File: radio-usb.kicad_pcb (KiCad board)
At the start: 2 copper layers, 127 x 90 mm, 228 parts, among them J1 Barrel_Jack, J10 Conn_Coaxial, J11 ACJS-MHDRM, J12 ACJS-MHDRM, J2 miniUSB, J3 15EDGRC-3.5-03P-14, J4 DB9_Female, J5 EEP_EN, J6 Mini-DIN-6, J7 EDAC 690-008-221-904, J8 DB9_Male, J9 Conn_Coaxial, Q1 BC846C, Q2 BC846, Q3 BC846, Q4 BC846, Q5 BC856, SW1 SW_Push_DPDT, SW2 SW_SPDT, SW3 SW_SPDT, SW4 SW_DIP_x04, SW5 SW_DIP_x04, SW6 SW_DPDT_x2, SW7 SW_SPDT, U1 L7805, U10 AP2171W, U11 TLP2662, U12 TLP2662, U13 MAX3232, U14 93CxxC, U15 PCM2902, U17 FT2232HL, U18 PC817, U19 CRIYCHLEY9000, U2 24LC04, U20 PC817, U21 PC817, U22 CRIYCHLEY9000, U23 LMV321IDBVR, U3 APX809_810-xxSA, U4 AP22814AW5, U5 AP22814AW5, U6 USB2514B_Bi, U7 LM1117-3.3, U8 TBA 1-0511, U9 4069, X1 MAB5SH, Y1 24MHz, Y2 12MHz, Y3 12M

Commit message: almost everything routed
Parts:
- moved TP8 32.2 mm to (174.0, 74.5)
- moved R71 20.4 mm to (115.1, 49.1), turned to 180 degrees
- moved R45 1.86 mm to (108.5, 49.8)
- moved C37 1.85 mm to (114.8, 43.9)
- moved C48 1.22 mm to (109.1, 64.6)
- moved R68 0.66 mm to (111.3, 64.8)
- moved Q4 0.57 mm to (133.5, 69.5)
- moved R63 0.49 mm to (134.1, 73.5)
- moved C39 0.45 mm to (117.2, 44.9)
- moved R53 0.40 mm to (111.8, 43.4)
- moved R72 0.36 mm to (111.3, 48.8)
- moved R64 0.33 mm to (111.3, 46.8)
- moved C62 0.20 mm to (124.4, 72.7)
- moved R66 0.05 mm to (122.3, 77.2)
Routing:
- net GND: track 298.3 -> 574.2 mm, vias 75 -> 93
- net GNDREF: track 144.4 -> 226.2 mm, vias 7 -> 9
- net /PTT_ACTL: track 0.00 -> 76.4 mm, vias 0 -> 1
- net RX_ACTIVE: track 15.3 -> 77.8 mm, vias 1 -> 3
- net /PTT_ACTH: track 0.00 -> 57.3 mm, vias 0 -> 3
- net /AF_FRM_RADIO_PREINS: track 68.4 -> 125.3 mm, vias 1 -> 4
- net /AUD_IN_SUM: track 69.5 -> 119.8 mm, vias 1 -> 4
- net /AUD_VDDI: track 0.00 -> 40.2 mm, vias 0 -> 2
- net /RX_ACT_SEP: track 27.4 -> 65.9 mm, vias 1 -> 4
- net /RCA_LEFT: track 50.5 -> 87.4 mm, vias 0 -> 3
- net /AUD_VBUS: track 8.70 -> 44.3 mm, vias 0 -> 2
- net /RCA_RIGHT: track 43.2 -> 78.8 mm, vias 0 -> 1
- net Net-(Q4-Pad3): track 9.07 -> 42.9 mm, vias 1 -> 5
- net VD: track 126.6 -> 155.6 mm, vias 4 -> 7
- net Net-(C63-Pad1): track 64.6 -> 90.0 mm, vias 0 -> 1
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
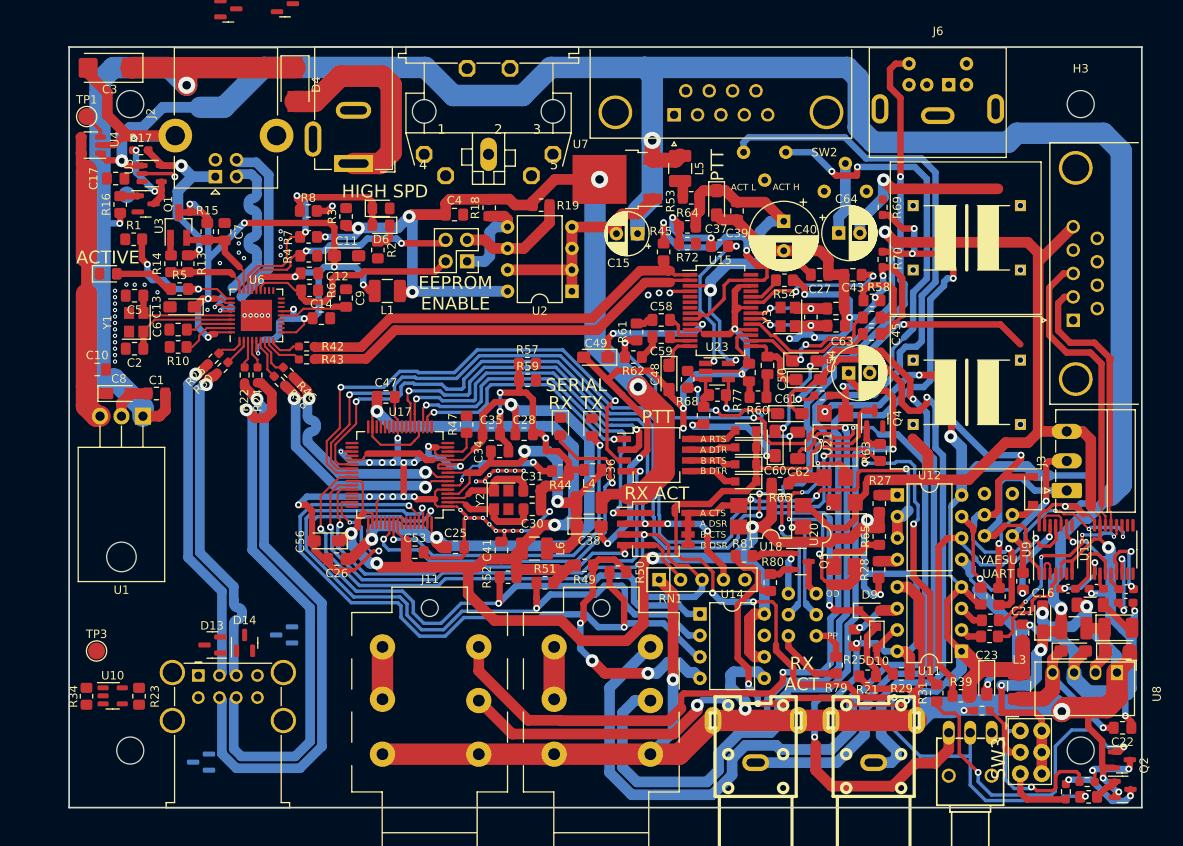
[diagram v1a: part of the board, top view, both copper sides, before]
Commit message: everything but ground poluygon and fixed bourns trafo pinout
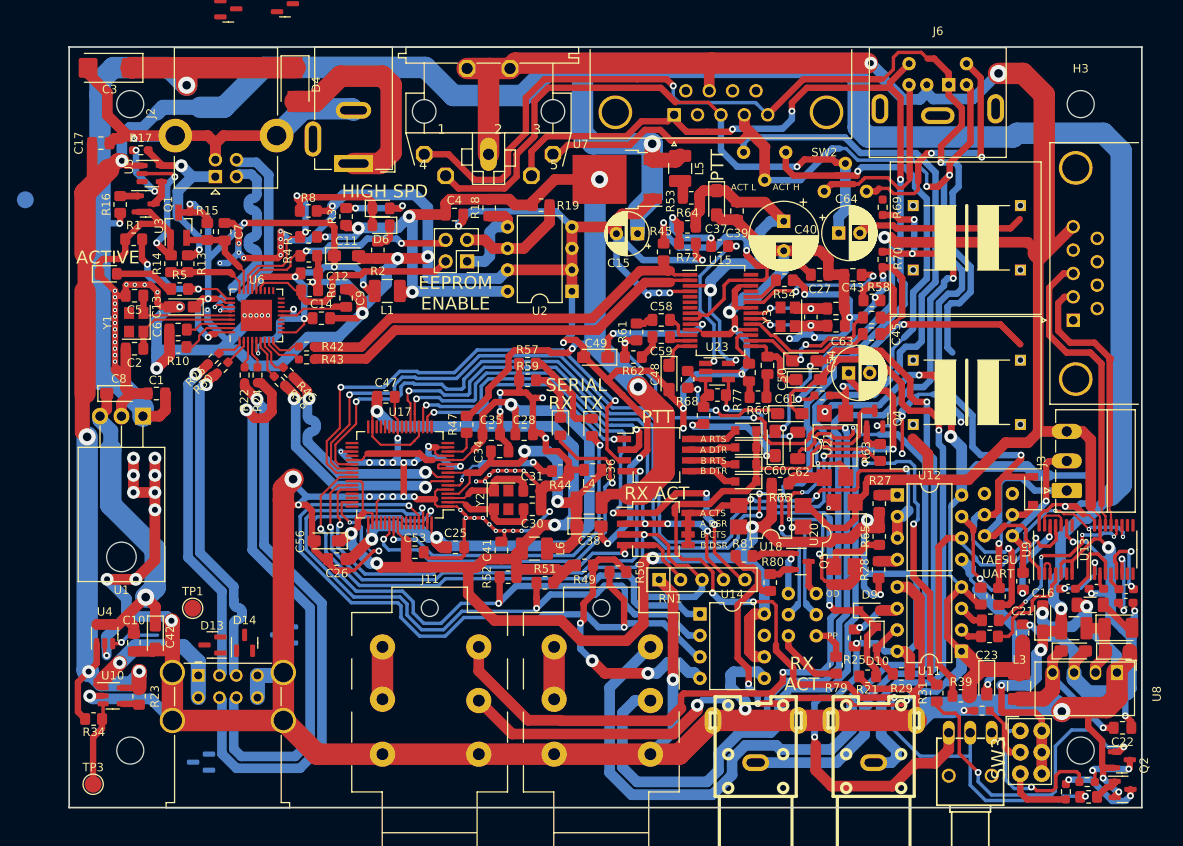
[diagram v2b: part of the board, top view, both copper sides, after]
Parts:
- added C42: 22u, Capacitor_Tantalum_SMD:CP_EIA-3216-18_Kemet-A_Pad1.58x1.35mm_HandSolder, F.Cu at (48.3, 95.4)
- moved TP1 59.6 mm to (52.7, 91.9)
- moved U4 57.9 mm to (42.3, 95.0), turned to 90 degrees
- moved C10 32.6 mm to (45.8, 96.0), turned to -90 degrees
- moved TP3 15.8 mm to (40.9, 112.8)
- moved TP2 12.0 mm to (32.9, 43.6)
- moved C17 4.54 mm to (41.9, 36.9)
- moved R34 2.82 mm to (41.0, 105.1), turned to 0 degrees
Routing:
- net GND: track 574.2 -> 1032.9 mm, vias 93 -> 122
- net AF_TO_RADIO: track 0.00 -> 119.4 mm, vias 0 -> 2
- net GNDREF: track 226.2 -> 332.4 mm, vias 9 -> 11
- net PTT: track 47.5 -> 146.4 mm, vias 2 -> 4
- net +5V: track 256.5 -> 351.4 mm, vias 5 -> 8
- net AF_FRM_RADIO: track 8.57 -> 72.3 mm, vias 0 -> 1
- net RX_ACTIVE: track 77.8 -> 128.4 mm, vias 3 -> 5
- net /YAESU_FILTERED_AUD: track 0.00 -> 30.4 mm, vias 0 -> 2
- net /YAESU_FLAT_AUD: track 0.00 -> 23.0 mm
- net +5VP: track 0.00 -> 22.4 mm, vias 0 -> 1
- net +3V3: track 109.0 -> 129.4 mm, vias 6 -> 7
- net /SER_A_CTS_IN: track 45.8 -> 65.9 mm, vias 2 -> 4
- net Net-(D15-Pad1): track 0.00 -> 10.8 mm
- net /+5VP_OK: track 0.00 -> 10.0 mm
- net Net-(D5-Pad2): track 0.00 -> 8.44 mm, vias 0 -> 2
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
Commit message: everything routed, bourns audio transformer footprint correcred, ground polygons
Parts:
- removed D11, D13, D14, D2, D3, D8: CM1213A-01SO, Package_TO_SOT_SMD:SOT-23
- added R56: 2k2, Resistor_SMD:R_0805_2012Metric_Pad1.20x1.40mm_HandSolder, B.Cu at (159.5, 72.7)
- TP1, TP6: footprint TestPoint:TestPoint_Pad_D2.0mm -> TestPoint:TestPoint_Pad_D1.0mm; moved to B.Cu
- TP2, TP4, TP5, TP9: footprint TestPoint:TestPoint_Pad_D2.0mm -> TestPoint:TestPoint_Pad_D1.0mm
- moved TP6 332.8 mm to (148.3, 88.6), turned to 180 degrees
- moved TP9 47.2 mm to (134.0, 94.5)
- moved TP8 40.5 mm to (133.6, 76.9)
- moved TP7 27.1 mm to (146.7, 95.5)
- moved TP5 23.9 mm to (151.0, 92.5)
- moved TP4 17.7 mm to (161.5, 81.2)
- moved TP2 11.6 mm to (44.5, 43.2)
- moved TP1 2.52 mm to (52.0, 94.4), turned to 180 degrees
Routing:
- net GND: track 1032.9 -> 1095.0 mm, vias 122 -> 123
- net /CAT_UART_RX: track 27.3 -> 43.9 mm, vias 0 -> 2
- net GNDREF: track 332.4 -> 341.3 mm
- net AF_TO_RADIO: track 119.4 -> 124.4 mm, vias 2 -> 3
- net Net-(TP2-Pad1): track 0.00 -> 4.69 mm, vias 0 -> 1
- net /SER_B_TXD_OUT: track 113.0 -> 117.3 mm
- net Net-(R69-Pad2): track 0.00 -> 3.90 mm
- net Net-(TP1-Pad1): track 5.72 -> 9.49 mm
- net /TTL_RX_2: track 12.5 -> 16.3 mm, vias 0 -> 1
- net Net-(C63-Pad2): track 22.7 -> 24.6 mm
- net /SER_B_RXD_IN: track 114.8 -> 116.6 mm, vias 2 -> 3
- net Net-(C64-Pad2): track 20.0 -> 21.6 mm
- net /TTL_RX: track 22.2 -> 23.6 mm
- net /TTL_TX: track 49.0 -> 50.1 mm
- net /TTL_TX_2: track 25.9 -> 27.0 mm
- added copper zone on B.Cu, net GND
- added copper zone on F.Cu, net GND
- added copper zone on B.Cu, net GNDREF
- added copper zone on F.Cu, net GNDREF

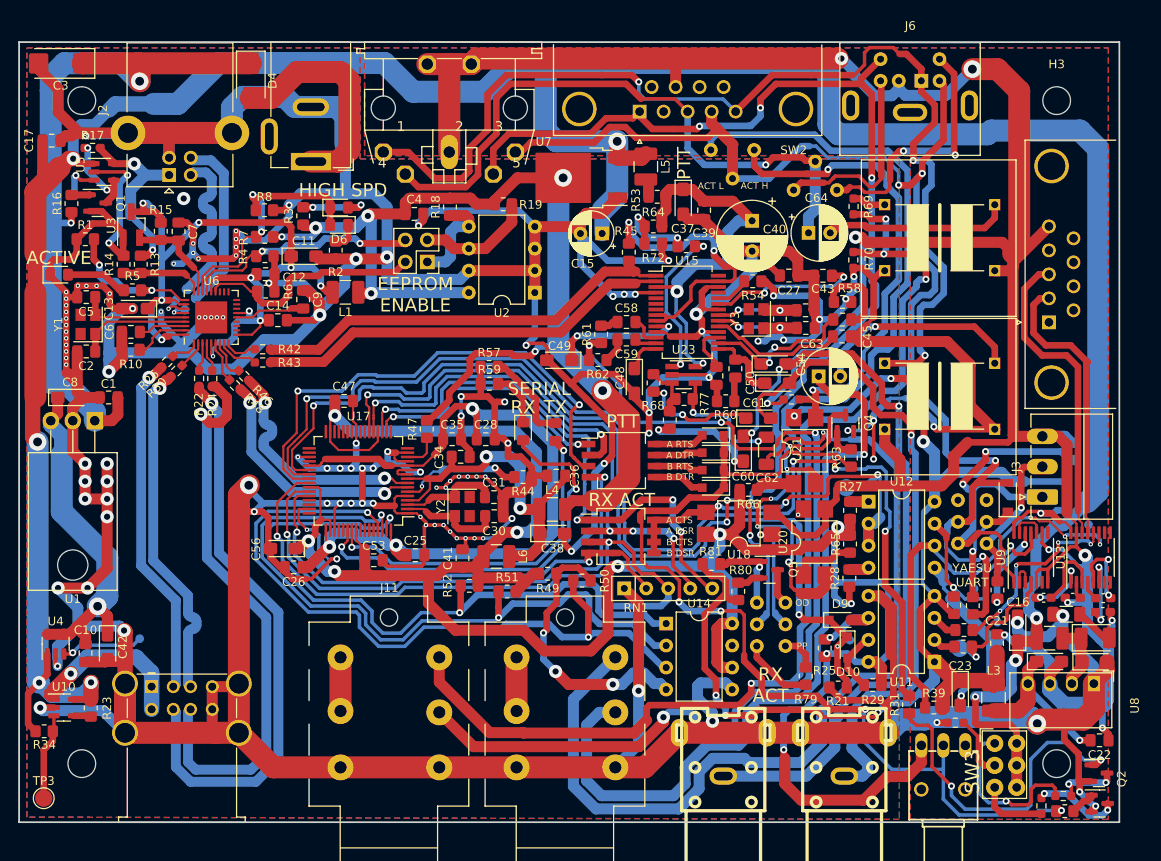
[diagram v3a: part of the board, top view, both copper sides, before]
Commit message: silkscreen description and test points
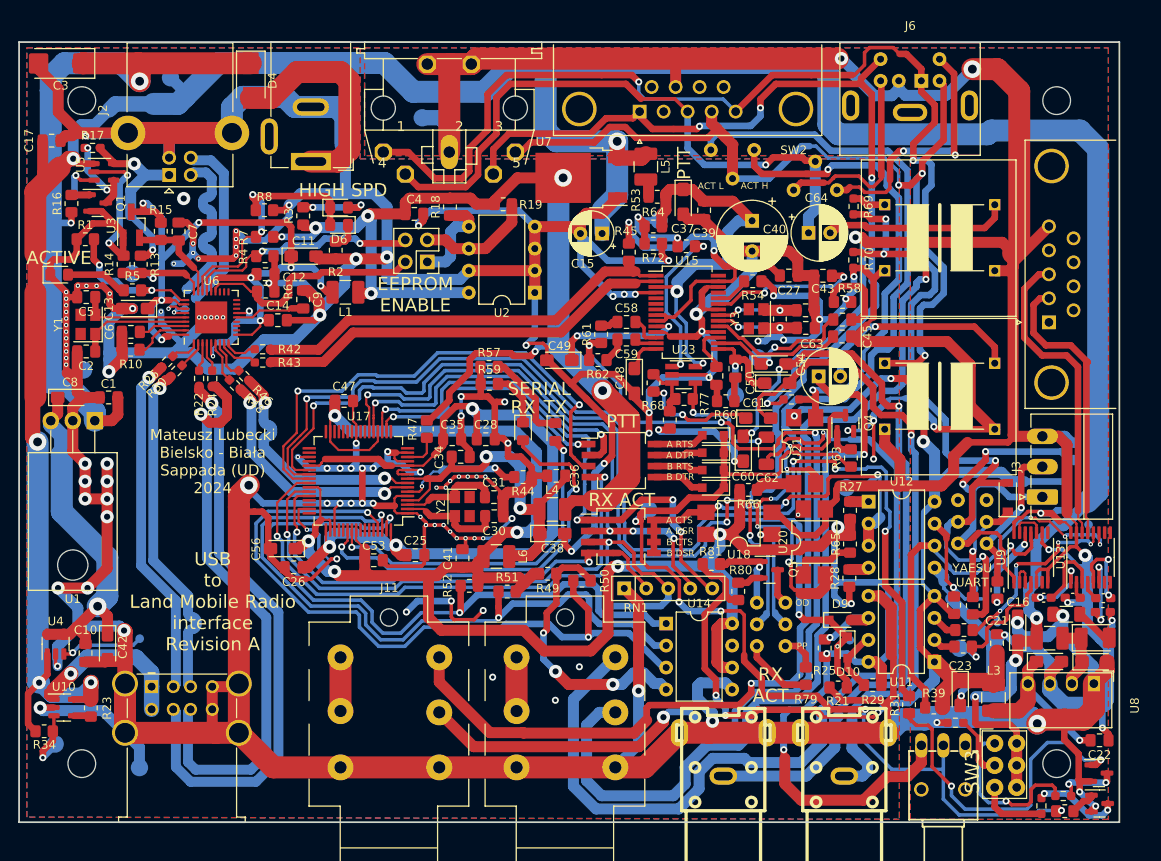
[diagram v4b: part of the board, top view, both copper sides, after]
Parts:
- added TP10: AUD_OUT_L, TestPoint:TestPoint_Pad_D2.0mm, B.Cu at (123.3, 61.9)
- added TP11: AUD_OUT_R, TestPoint:TestPoint_Pad_D2.0mm, B.Cu at (120.8, 66.3)
- added TP12: OPAMP_BIAS, TestPoint:TestPoint_Pad_D2.0mm, B.Cu at (112.0, 46.1)
- added TP13: PTT_CTRL, TestPoint:TestPoint_Pad_D2.0mm, B.Cu at (110.8, 79.5)
- added TP14: USB_GROUND, TestPoint:TestPoint_Pad_D2.0mm, B.Cu at (52.0, 109.2)
- added TP15: GROUND, TestPoint:TestPoint_Pad_D2.0mm, B.Cu at (84.6, 34.2)
- added TP16: +12V, TestPoint:TestPoint_Pad_D2.0mm, B.Cu at (45.5, 63.3)
- added TP17: +2V5, TestPoint:TestPoint_Pad_D2.0mm, B.Cu at (51.2, 52.2)
- added TP18: +5V, TestPoint:TestPoint_Pad_D2.0mm, B.Cu at (55.6, 29.6)
- TP3: moved to B.Cu
- moved TP3 6.39 mm to (42.3, 106.5), turned to 180 degrees
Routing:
- net GND: track 1095.0 -> 1110.2 mm, vias 123 -> 128
- net GNDREF: track 341.3 -> 347.8 mm
- net /AUD_OUT_RIGHT: track 8.52 -> 13.2 mm, vias 0 -> 1
- net +12V: track 85.1 -> 88.4 mm
- net +2V5: track 9.64 -> 12.9 mm, vias 0 -> 1
- net +5V: track 351.4 -> 354.3 mm
- net /PTT_CTRL: track 114.1 -> 116.7 mm, vias 4 -> 5
- net Net-(R64-Pad1): track 10.6 -> 13.3 mm
- net /+5VP_OK: track 10.0 -> 7.65 mm, vias 0 -> 1
- net /AUD_OUT_LEFT: track 18.0 -> 19.6 mm
- net /SER_VCCIO: track 279.7 -> 280.7 mm
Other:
- board text added: "+12V"
- board text added: "+12V_FLG"
- board text added: "+2V5"
- board text added: "+5V"
- board text added: "+5VP_OK"
- board text added: "AUD_OUT_L"
- board text added: "AUD_OUT_R"
- board text added: "Audio Left"
- board text added: "Audio Right"
- board text added: "DB9 pinout 1 - RX active in / CTCSS status in 3 - Audio from radio 4 - PTT out 5 - Audio to radio 7 - Ground"
- board text added: "DIN5 pinout 1 - Audio to radio 2 - Ground 3 - PTT out 4 - Audio from radio 5 - RX active in / CTCSS status in"
- board text added: "GND"
- board text added: "GROUND"
- board text added: "INSERT Audio From Radio"
- board text added: "INSERT Audio To Radio"
- board text added: "Isolated RS232"
- board text added: "Mateusz Lubecki Bielsko - Biała Sappada (UD) 2024"
- board text added: "OPAMP_BIAS"
- board text added: "PTT_CTRL"
- board text added: "SER_B_RXD_IN"
- board text added: "SER_B_TXD_OUT"
- board text added: "TIP - Send RING - Return SLEEVE - Ground"
- board text added: "TTL_RX"
- board text added: "TTL_RX_2"
- board text added: "TTL_TX"
- board text added: "TTL_TX_2"
- board text added: "These Audio connectors are on non-isolated USB ground"
- board text added: "USB to Land Mobile Radio interface Revision A"
- board text added: "USB_GROUND"
- board text added: "VBUS_FLG"
- board text added: "isolated TTL-UART"
- board text added: "miniDIN6 Yaesu 7800/8800/8900 pinout"

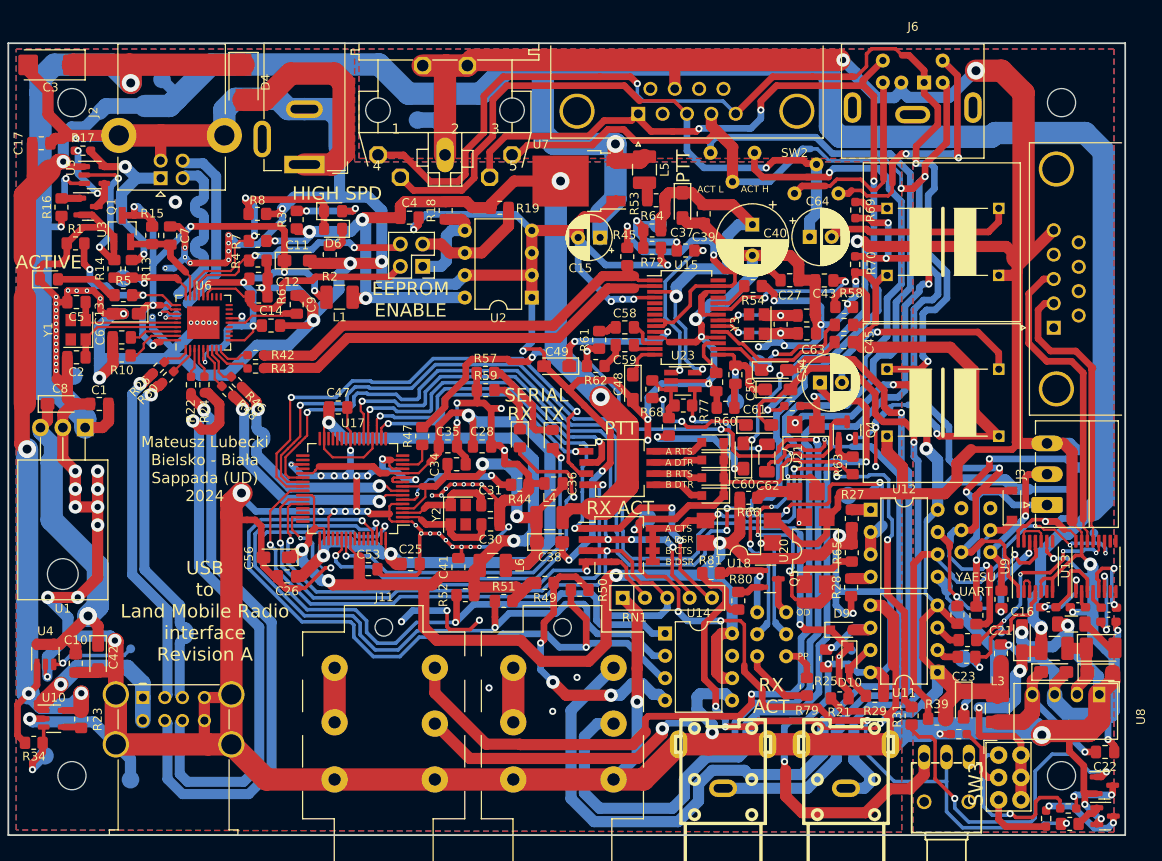
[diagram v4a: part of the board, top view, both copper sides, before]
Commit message: fixed mini din 6 orientation, fix via size problems
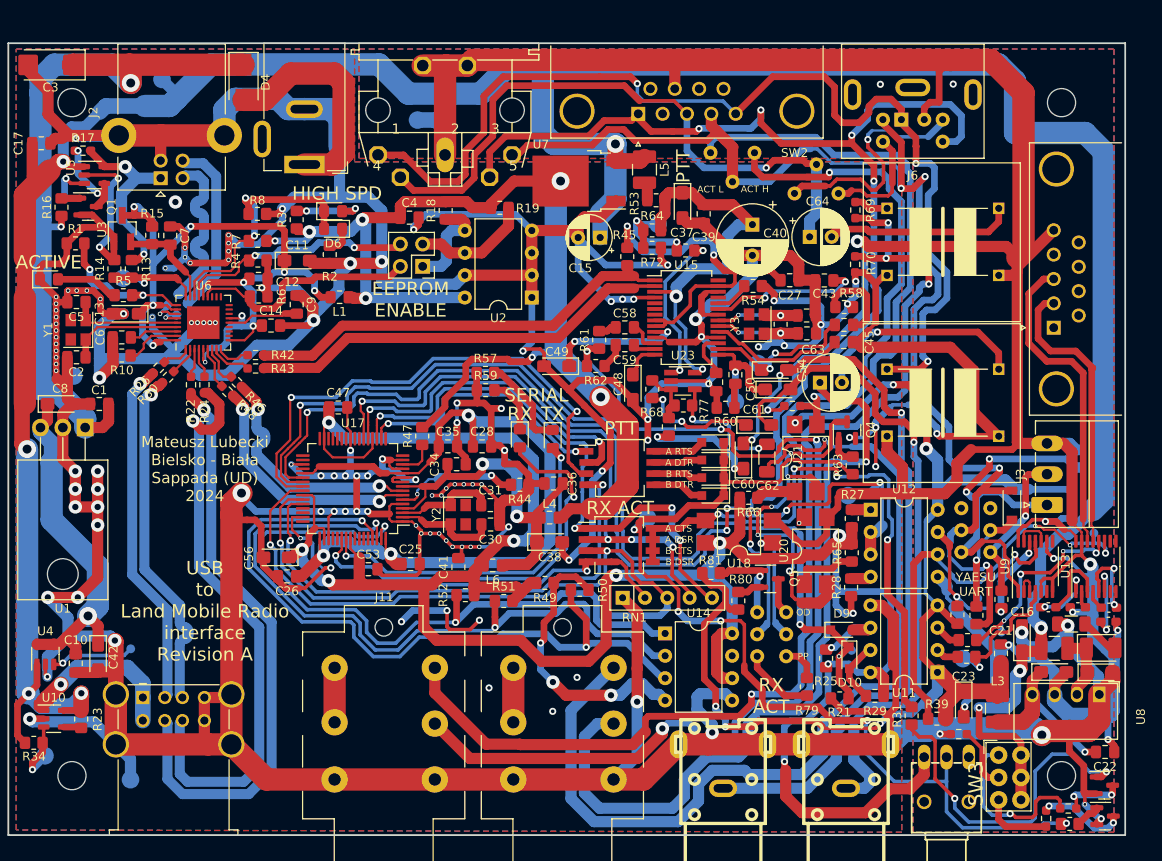
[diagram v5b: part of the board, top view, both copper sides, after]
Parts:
- C30, C31: value 27pF -> 30pF
- L1, L4, L6: footprint Inductor_SMD:L_1210_3225Metric_Pad1.42x2.65mm_HandSolder -> Inductor_SMD:L_0805_2012Metric_Pad1.15x1.40mm_HandSolder
- Q2, Q3, Q4: value BC846 -> BC846C
- U6: value USB2514B_Bi -> USB2514B-AEZC
- moved J6 4.95 mm to (139.6, 34.2), turned to 180 degrees
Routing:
- net /YAESU_FILTERED_AUD: track 30.4 -> 13.3 mm, vias 2 -> 0
- net RX_ACTIVE: track 128.4 -> 138.7 mm, vias 5 -> 6
- net AF_TO_RADIO: track 124.4 -> 119.3 mm
- net /YAESU_FLAT_AUD: track 23.0 -> 27.8 mm, vias 0 -> 1
- net GNDREF: track 347.8 -> 352.5 mm
- net PTT: track 146.4 -> 143.5 mm

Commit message: gerber files and another fabrication output
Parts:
- R27, R28, R32, R33, R79, R80: value 660 -> 680
- U15: value PCM2902 -> PCM2900CDB
